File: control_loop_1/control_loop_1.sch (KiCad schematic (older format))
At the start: 62 parts, among them J1 I_MEAS, J10 GND, J11 -5V, J12 POW_OUT, J13 I_SET, J14 U_SET, J15 GND, J16 CTR_MODE, J17 GND, J18 CTR_MODE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

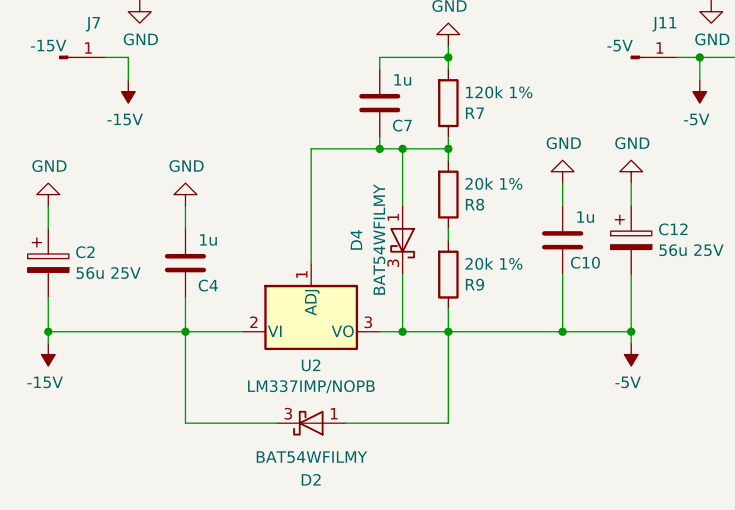
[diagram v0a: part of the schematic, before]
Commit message: fixed diodes orientation
negative volt regulator - reversed diodes fixed
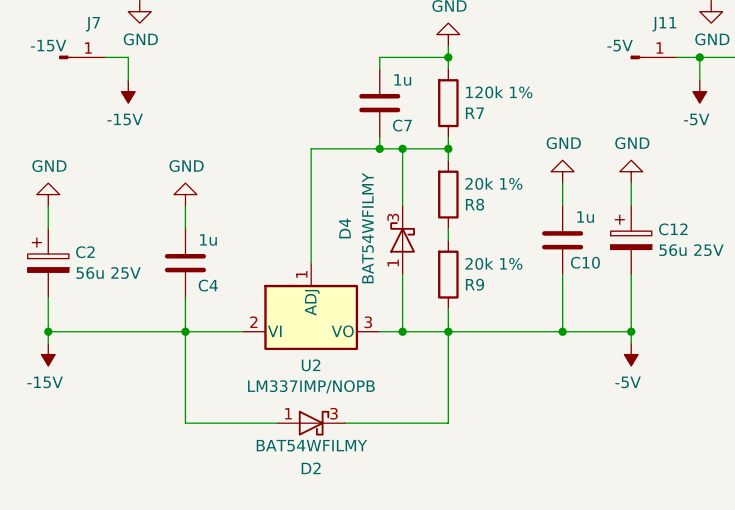
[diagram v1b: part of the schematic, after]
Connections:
- net -15V: now also D2.1 (A); no longer D2.3 (K)
- net -5V: now also D2.3 (K), D4.1 (A); no longer D2.1 (A), D4.3 (K)
- net at C7.2, R7.1, R8.2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: now also D4.3 (K); no longer D4.1 (A)
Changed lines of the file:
@@
 AR Path="/5F803A87/5F8AA148" Ref="D?"  Part="1"
 AR Path="/5F8AA148" Ref="D4"  Part="1"
-F 0 "D4" H 2250 6450 50  0000 C CNN
-F 1 "BAT54WFILMY" H 2250 6550 50  0000 C CNN
+F 0 "D4" H 2200 6900 50  0000 C CNN
+F 1 "BAT54WFILMY" H 2200 6800 50  0000 C CNN
 F 2 "Package_TO_SOT_SMD:SOT-323_SC-70" H 2250 6475 50  0001 C CNN
 F 3 "https://pl.mouser.com/datasheet/2/389/cd00278204-1797144.pdf" H 2250 6650 50  0001 C CNN
 	1    2250 6650
-	0    1    -1   0
+	0    -1   1    0
 $EndComp
 Wire Wire Line
@@
 AR Path="/5F803A87/5F8AA164" Ref="D?"  Part="1"
 AR Path="/5F8AA164" Ref="D2"  Part="1"
-F 0 "D2" H 1850 7700 50  0000 C CNN
-F 1 "BAT54WFILMY" H 1850 7600 50  0000 C CNN
+F 0 "D2" H 1850 7250 50  0000 C CNN
+F 1 "BAT54WFILMY" H 1850 7350 50  0000 C CNN
 F 2 "Package_TO_SOT_SMD:SOT-323_SC-70" H 1850 7275 50  0001 C CNN
 F 3 "https://pl.mouser.com/datasheet/2/389/cd00278204-1797144.pdf" H 1850 7450 50  0001 C CNN
 	1    1850 7450
-	1    0    0    1
+	-1   0    0    -1
 $EndComp
 Wire Wire Line
